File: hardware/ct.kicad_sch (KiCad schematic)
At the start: 34 parts, among them J1 Banana, J2 Banana, J3 Pin Header Male, SW1 Tactile Button, U1 TLV431, U2 TLV333, U3 ATmega88PA-A

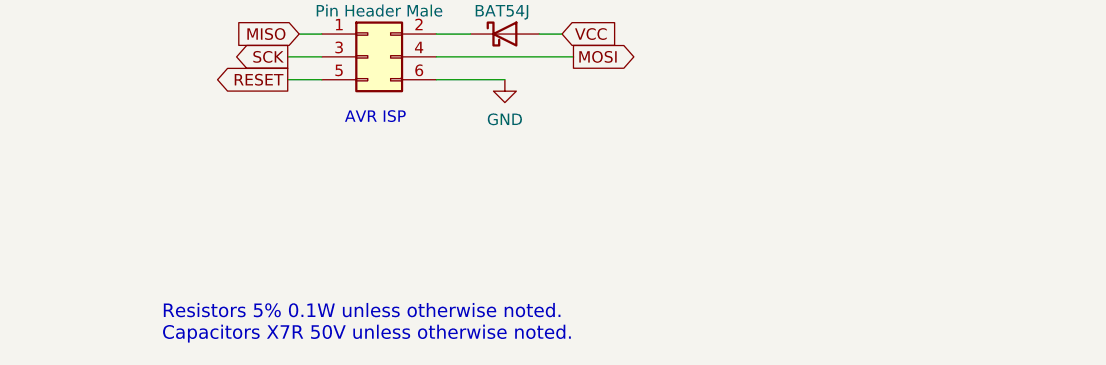
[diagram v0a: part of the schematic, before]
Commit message: Add alternatives for U2
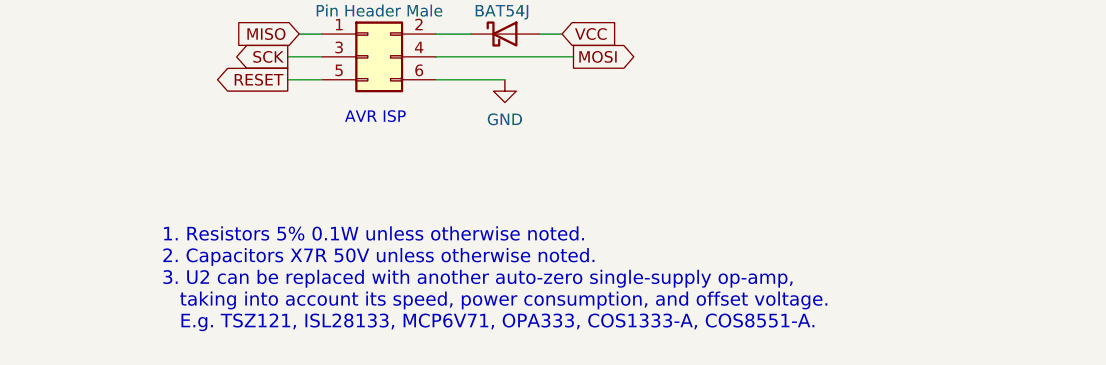
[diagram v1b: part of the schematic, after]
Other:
- note added: "1. Resistors 5% 0.1W unless otherwise noted. 2. Capacitors X7R 50V unless otherwise noted. 3. U2 can be replaced with another auto-zero single-supply op-amp, taking into account its speed, power consumption, and offset voltage. E.g. TSZ121, ISL28133, MCP6V71, OPA333, COS1333-A, COS8551-A."
- note removed: "Resistors 5% 0.1W unless otherwise noted. Capacitors X7R 50V unless otherwise noted."
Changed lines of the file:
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@@
     (effects (font (size 1.27 1.27)) (justify left bottom))
   )
-  (text "Resistors 5% 0.1W unless otherwise noted.\nCapacitors X7R 50V unless otherwise noted."
-    (at 177.8 180.34 0)
+  (text "1. Resistors 5% 0.1W unless otherwise noted.\n2. Capacitors X7R 50V unless otherwise noted.\n3. U2 can be replaced with another auto-zero single-supply op-amp,\n   taking into account its speed, power consumption, and offset voltage.\n   E.g. TSZ121, ISL28133, MCP6V71, OPA333, COS1333-A, COS8551-A.\n"
+    (at 177.8 179.07 0)
     (effects (font (size 1.5 1.5)) (justify left bottom))
   )

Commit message: Change U2 to MCP6V61
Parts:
- U2: value TLV333 -> MCP6V61
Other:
- note added: "1. Resistors 5% 0.1W unless otherwise noted. 2. Capacitors X7R 50V unless otherwise noted. 3. U2 can be replaced with another auto-zero single-supply op-amp, taking into account its speed, power consumption, and offset voltage. E.g. TLV333, ISL28133, TSZ121, COS1333-A, COS8551-A."
- note removed: "1. Resistors 5% 0.1W unless otherwise noted. 2. Capacitors X7R 50V unless otherwise noted. 3. U2 can be replaced with another auto-zero single-supply op-amp, taking into account its speed, power consumption, and offset voltage. E.g. TSZ121, ISL28133, MCP6V71, OPA333, COS1333-A, COS8551-A."
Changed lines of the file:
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@@
     (effects (font (size 1.27 1.27)) (justify left bottom))
   )
-  (text "1. Resistors 5% 0.1W unless otherwise noted.\n2. Capacitors X7R 50V unless otherwise noted.\n3. U2 can be replaced with another auto-zero single-supply op-amp,\n   taking into account its speed, power consumption, and offset voltage.\n   E.g. TSZ121, ISL28133, MCP6V71, OPA333, COS1333-A, COS8551-A.\n"
+  (text "1. Resistors 5% 0.1W unless otherwise noted.\n2. Capacitors X7R 50V unless otherwise noted.\n3. U2 can be replaced with another auto-zero single-supply op-amp,\n   taking into account its speed, power consumption, and offset voltage.\n   E.g. TLV333, ISL28133, TSZ121, COS1333-A, COS8551-A.\n"
     (at 177.8 179.07 0)
     (effects (font (size 1.5 1.5)) (justify left bottom))
@@
       (effects (font (size 1.27 1.27)))
     )
-    (property "Value" "TLV333" (at 99.06 88.9 0)
+    (property "Value" "MCP6V61" (at 100.33 88.9 0)
       (effects (font (size 1.27 1.27)))
     )

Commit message: Add reverse polarity protection for battery
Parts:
- added Q1: AO3423, Package_TO_SOT_SMD:SOT-23, symbol Transistor_FET:AO3401A
- C3: now left out of the parts list
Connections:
- net GND: now also Q1.1 (G)
- net VCC: now also Q1.2 (S); no longer BT1.1 (+)
- new net: BT1.1 (+), Q1.3 (D)
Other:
- moved on the sheet: BT1

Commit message: Add bypass to the reverse polarity protection
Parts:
- added R16: 0, Resistor_SMD:R_0603_1608Metric, symbol Device:R
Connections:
- net VCC: now also R16.2
- net at BT1.1 (+), Q1.3 (D): now also R16.1
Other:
- moved on the sheet: BT1
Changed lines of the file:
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@@
 	(title_block
 		(title "Continuity Tester")
-		(rev "2")
+		(rev "3")
 	)
 	(text "100 mV/Ω"
@@
 	)
 	(junction
+		(at 57.15 140.97)
+		(diameter 0)
+		(color 0 0 0 0)
+	)
+	(junction
 		(at 175.895 55.88)
 		(diameter 0)
@@
 	)
 	(junction
+		(at 82.55 140.97)
+		(diameter 0)
+		(color 0 0 0 0)
+	)
+	(junction
 		(at 118.11 92.71)
 		(diameter 0)
@@
 	(wire
 		(pts
-			(xy 80.01 140.97) (xy 83.82 140.97)
+			(xy 80.01 140.97) (xy 82.55 140.97)
 		)
 		(stroke
@@
 	(wire
 		(pts
+			(xy 82.55 135.89) (xy 82.55 140.97)
+		)
+		(stroke
+			(width 0)
+			(type default)
+		)
+	)
+	(wire
+		(pts
 			(xy 60.96 36.195) (xy 64.135 36.195)
 		)
@@
 	(wire
 		(pts
+			(xy 57.15 142.24) (xy 57.15 140.97)
+		)
+		(stroke
+			(width 0)
+			(type default)
+		)
+	)
+	(wire
+		(pts
 			(xy 191.77 148.59) (xy 195.58 148.59)
 		)
@@
 	(wire
 		(pts
+			(xy 57.15 135.89) (xy 59.69 135.89)
+		)
+		(stroke
+			(width 0)
+			(type default)
+		)
+	)
+	(wire
+		(pts
 			(xy 236.855 66.04) (xy 241.3 66.04)
 		)
@@
 	(wire
 		(pts
+			(xy 82.55 140.97) (xy 86.36 140.97)
+		)
+		(stroke
+			(width 0)
+			(type default)
+		)
+	)
+	(wire
+		(pts
 			(xy 78.105 46.355) (xy 74.295 46.355)
 		)
@@
 	(wire
 		(pts
+			(xy 67.31 135.89) (xy 82.55 135.89)
+		)
+		(stroke
+			(width 0)
+			(type default)
+		)
+	)
+	(wire
+		(pts
 			(xy 185.42 32.385) (xy 188.595 32.385)
 		)
@@
 	(wire
 		(pts
+			(xy 57.15 135.89) (xy 57.15 140.97)
+		)
+		(stroke
+			(width 0)
+			(type default)
+		)
+	)
+	(wire
+		(pts
 			(xy 209.55 32.385) (xy 204.47 32.385)
 		)
@@
 	(wire
 		(pts
+			(xy 74.93 149.86) (xy 74.93 148.59)
+		)
+		(stroke
+			(width 0)
+			(type default)
+		)
+	)
+	(wire
+		(pts
 			(xy 118.11 102.87) (xy 118.11 101.6)
 		)
@@
 	(global_label "VCC"
 		(shape output)
-		(at 83.82 140.97 0)
+		(at 86.36 140.97 0)
 		(fields_autoplaced yes)
 		(effects
@@
 		)
 		(property "Intersheetrefs" "${INTERSHEET_REFS}"
-			(at 90.3544 140.97 0)
+			(at 92.8944 140.97 0)
 			(effects
 				(font
@@
 	(symbol
 		(lib_id "power:GND")
-		(at 57.15 148.59 0)
+		(at 57.15 149.86 0)
 		(unit 1)
 		(exclude_from_sim no)
@@
 		(dnp no)
 		(property "Reference" "#PWR03"
-			(at 57.15 154.94 0)
+			(at 57.15 156.21 0)
 			(effects
 				(font
@@
 		)
 		(property "Value" "GND"
-			(at 57.15 153.035 0)
+			(at 57.15 154.305 0)
 			(effects
 				(font
@@
 		)
 		(property "Footprint" ""
-			(at 57.15 148.59 0)
+			(at 57.15 149.86 0)
 			(effects
 				(font
@@
 		)
 		(property "Datasheet" ""
-			(at 57.15 148.59 0)
+			(at 57.15 149.86 0)
 			(effects
 				(font
@@
 		)
 		(property "Description" ""
-			(at 57.15 148.59 0)
+			(at 57.15 149.86 0)
 			(effects
 				(font
@@
 		(lib_name "GND_1")
 		(lib_id "power:GND")
-		(at 74.93 148.59 0)
+		(at 74.93 149.86 0)
 		(unit 1)
 		(exclude_from_sim no)
@@
 		(fields_autoplaced yes)
 		(property "Reference" "#PWR020"
-			(at 74.93 154.94 0)
+			(at 74.93 156.21 0)
 			(effects
 				(font
@@
 		)
 		(property "Value" "GND"
-			(at 74.93 153.67 0)
+			(at 74.93 154.94 0)
 			(effects
 				(font
@@
 		)
 		(property "Footprint" ""
-			(at 74.93 148.59 0)
+			(at 74.93 149.86 0)
 			(effects
 				(font
@@
 		)
 		(property "Datasheet" ""
-			(at 74.93 148.59 0)
+			(at 74.93 149.86 0)
 			(effects
 				(font
@@
 		)
 		(property "Description" "Power symbol creates a global label with name \"GND\" , ground"
-			(at 74.93 148.59 0)
+			(at 74.93 149.86 0)
 			(effects
 				(font
@@
 	(symbol
 		(lib_id "Device:R")
+		(at 63.5 135.89 90)
+		(unit 1)
+		(exclude_from_sim no)
+		(in_bom no)
+		(on_board yes)
+		(dnp yes)
+		(property "Reference" "R16"
+			(at 63.5 130.81 90)
+			(effects
+				(font
+					(size 1.27 1.27)
+				)
+			)
+		)
+		(property "Value" "0"
+			(at 63.5 133.35 90)
+			(effects
+				(font
+					(size 1.27 1.27)
+				)
+			)
+		)
+		(property "Footprint" "Resistor_SMD:R_0603_1608Metric"
+			(at 63.5 137.668 90)
+			(effects
+				(font
+					(size 1.27 1.27)
+				)
+				(hide yes)
+			)
+		)
+		(property "Datasheet" "~"
+			(at 63.5 135.89 0)
+			(effects
+				(font
+					(size 1.27 1.27)
+				)
+				(hide yes)
+			)
+		)
+		(property "Description" ""
+			(at 63.5 135.89 0)
+			(effects
+				(font
+					(size 1.27 1.27)
+				)
+			)
+		)
+		(pin "1"
+		)
+		(pin "2"
+		)
+		(instances
+			(project "ct"
+				(path "/b6242731-dc1d-4d55-82cb-38d098140970"
+					(reference "R16")
+					(unit 1)
+				)
+			)
+		)
+	)
+	(symbol
+		(lib_id "Device:R")
 		(at 168.275 55.88 270)
 		(unit 1)
@@
 	(symbol
 		(lib_id "Device:Battery_Cell")
-		(at 57.15 146.05 0)
+		(at 57.15 147.32 0)
 		(unit 1)
 		(exclude_from_sim no)
@@
 		(dnp no)
 		(property "Reference" "BT1"
-			(at 60.452 143.51 0)
+			(at 60.452 144.78 0)
 			(effects
 				(font
@@
 		)
 		(property "Value" "CR2032"
-			(at 60.452 146.05 0)
+			(at 60.452 147.32 0)
 			(effects
 				(font
@@
 		)
 		(property "Footprint" "Battery:BatteryHolder_MPD_BC2003_1x2032"
-			(at 57.15 144.526 90)
+			(at 57.15 145.796 90)
 			(effects
 				(font
@@
 		)
 		(property "Datasheet" "~"
-			(at 57.15 144.526 90)
+			(at 57.15 145.796 90)
 			(effects
 				(font
@@
 		)
 		(property "Description" ""
-			(at 57.15 146.05 0)
+			(at 57.15 147.32 0)
 			(effects
 				(font
@@
 		(on_board yes)
 		(dnp no)
-		(fields_autoplaced yes)
 		(property "Reference" "Q1"
-			(at 74.93 134.62 90)
+			(at 79.756 143.51 90)
 			(effects
 				(font
@@
 		)
 		(property "Value" "AO3423"
-			(at 74.93 137.16 90)
+			(at 80.01 146.05 90)
 			(effects
 				(font
